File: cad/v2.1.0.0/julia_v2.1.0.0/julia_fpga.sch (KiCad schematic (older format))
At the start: 28 parts, among them U1 EP4CE6F17, X1 50MHz

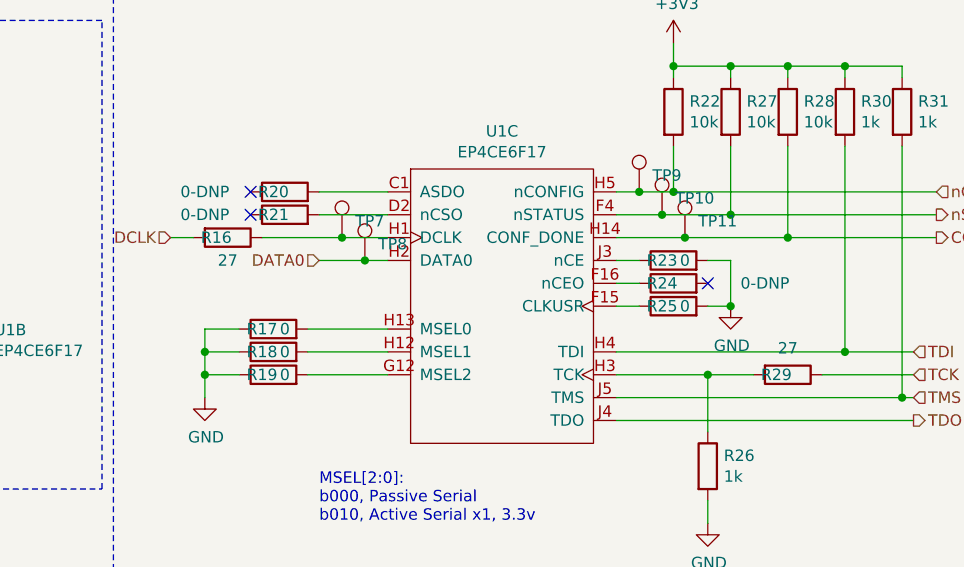
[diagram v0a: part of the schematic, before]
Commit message: v2.1.0.0: changed connector, ERC, annotation/footprint assignment
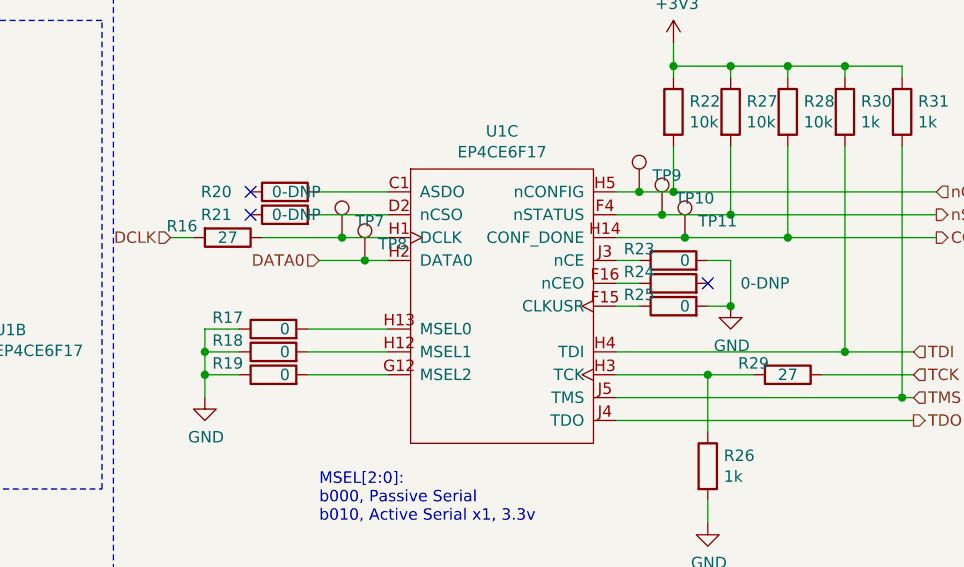
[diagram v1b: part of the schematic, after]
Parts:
- C46: footprint (none) -> Capacitor_Tantalum_SMD:CP_EIA-2012-15_AVX-P
- C47: footprint (none) -> Capacitor_SMD:C_0402_1005Metric
- FB1: footprint (none) -> Inductor_SMD:L_0603_1608Metric
- R15, R16, R17, R18, R19, R20, R21, R22, R23, R24, R25, R26, R27, R28, R29, R30, R31: footprint (none) -> Resistor_SMD:R_0402_1005Metric
- TP10, TP11, TP6, TP7, TP8, TP9: footprint (none) -> TestPoint:TestPoint_THTPad_D1.0mm_Drill0.5mm
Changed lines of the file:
@@
 F 0 "TP6" H 5758 1672 50  0000 L CNN
 F 1 "TestPoint" H 5758 1627 50  0001 L CNN
-F 2 "" H 5900 1600 50  0001 C CNN
+F 2 "TestPoint:TestPoint_THTPad_D1.0mm_Drill0.5mm" H 5900 1600 50  0001 C CNN
 F 3 "~" H 5900 1600 50  0001 C CNN
 	1    5700 1600
@@
 F 0 "C46" H 3518 1796 50  0000 L CNN
 F 1 "4.7uF" H 3518 1705 50  0000 L CNN
-F 2 "" H 3438 1600 50  0001 C CNN
+F 2 "Capacitor_Tantalum_SMD:CP_EIA-2012-15_AVX-P" H 3438 1600 50  0001 C CNN
 F 3 "~" H 3400 1750 50  0001 C CNN
 	1    3400 1750
@@
 F 0 "C47" H 3965 1796 50  0000 L CNN
 F 1 "0.1uF" H 3965 1705 50  0000 L CNN
-F 2 "" H 3888 1600 50  0001 C CNN
+F 2 "Capacitor_SMD:C_0402_1005Metric" H 3888 1600 50  0001 C CNN
 F 3 "~" H 3850 1750 50  0001 C CNN
 	1    3850 1750
@@
 F 0 "FB1" H 3500 1346 50  0000 L CNN
 F 1 "600R/1A" H 3500 1255 50  0000 L CNN
-F 2 "" V 3330 1300 50  0001 C CNN
+F 2 "Inductor_SMD:L_0603_1608Metric" V 3330 1300 50  0001 C CNN
 F 3 "~" H 3400 1300 50  0001 C CNN
 	1    3400 1300
@@
 F 0 "R15" V 5193 1850 50  0000 C CNN
 F 1 "27" V 5284 1850 50  0000 C CNN
-F 2 "" V 5330 1850 50  0001 C CNN
+F 2 "Resistor_SMD:R_0402_1005Metric" V 5330 1850 50  0001 C CNN
 F 3 "~" H 5400 1850 50  0001 C CNN
 	1    5400 1850
@@
 F 0 "TP9" H 9408 1572 50  0000 L CNN
 F 1 "TestPoint" H 9408 1527 50  0001 L CNN
-F 2 "" H 9550 1500 50  0001 C CNN
+F 2 "TestPoint:TestPoint_THTPad_D1.0mm_Drill0.5mm" H 9550 1500 50  0001 C CNN
 F 3 "~" H 9550 1500 50  0001 C CNN
 	1    9350 1500
@@
 F 0 "TP11" H 9608 1772 50  0000 L CNN
 F 1 "TestPoint" H 9608 1727 50  0001 L CNN
-F 2 "" H 9750 1700 50  0001 C CNN
+F 2 "TestPoint:TestPoint_THTPad_D1.0mm_Drill0.5mm" H 9750 1700 50  0001 C CNN
 F 3 "~" H 9750 1700 50  0001 C CNN
 	1    9550 1700
@@
 F 0 "TP10" H 9508 1672 50  0000 L CNN
 F 1 "TestPoint" H 9508 1627 50  0001 L CNN
-F 2 "" H 9650 1600 50  0001 C CNN
+F 2 "TestPoint:TestPoint_THTPad_D1.0mm_Drill0.5mm" H 9650 1600 50  0001 C CNN
 F 3 "~" H 9650 1600 50  0001 C CNN
 	1    9450 1600
@@
 U 1 1 604BBA22
 P 10000 2300
-F 0 "R29" V 10000 2250 50  0000 C CNN
-F 1 "27" V 9884 2300 50  0000 C CNN
-F 2 "" V 9930 2300 50  0001 C CNN
+F 0 "R29" V 9950 2150 50  0000 C CNN
+F 1 "27" V 10000 2300 50  0000 C CNN
+F 2 "Resistor_SMD:R_0402_1005Metric" V 9930 2300 50  0001 C CNN
 F 3 "~" H 10000 2300 50  0001 C CNN
 	1    10000 2300
@@
 F 0 "R26" H 9720 2746 50  0000 L CNN
 F 1 "1k" H 9720 2655 50  0000 L CNN
-F 2 "" V 9580 2700 50  0001 C CNN
+F 2 "Resistor_SMD:R_0402_1005Metric" V 9580 2700 50  0001 C CNN
 F 3 "~" H 9650 2700 50  0001 C CNN
 	1    9650 2700
@@
 F 0 "R30" H 10320 1196 50  0000 L CNN
 F 1 "1k" H 10320 1105 50  0000 L CNN
-F 2 "" V 10180 1150 50  0001 C CNN
+F 2 "Resistor_SMD:R_0402_1005Metric" V 10180 1150 50  0001 C CNN
 F 3 "~" H 10250 1150 50  0001 C CNN
 	1    10250 1150
@@
 F 0 "R31" H 10570 1196 50  0000 L CNN
 F 1 "1k" H 10570 1105 50  0000 L CNN
-F 2 "" V 10430 1150 50  0001 C CNN
+F 2 "Resistor_SMD:R_0402_1005Metric" V 10430 1150 50  0001 C CNN
 F 3 "~" H 10500 1150 50  0001 C CNN
 	1    10500 1150
@@
 U 1 1 60569DDE
 P 7750 2100
-F 0 "R17" V 7750 2150 50  0000 C CNN
+F 0 "R17" V 7800 2300 50  0000 C CNN
 F 1 "0" V 7750 2050 50  0000 C CNN
-F 2 "" V 7680 2100 50  0001 C CNN
+F 2 "Resistor_SMD:R_0402_1005Metric" V 7680 2100 50  0001 C CNN
 F 3 "~" H 7750 2100 50  0001 C CNN
 	1    7750 2100
@@
 U 1 1 60576BC4
 P 7750 2200
-F 0 "R18" V 7750 2250 50  0000 C CNN
+F 0 "R18" V 7800 2400 50  0000 C CNN
 F 1 "0" V 7750 2150 50  0000 C CNN
-F 2 "" V 7680 2200 50  0001 C CNN
+F 2 "Resistor_SMD:R_0402_1005Metric" V 7680 2200 50  0001 C CNN
 F 3 "~" H 7750 2200 50  0001 C CNN
 	1    7750 2200
@@
 U 1 1 605775E4
 P 7750 2300
-F 0 "R19" V 7750 2350 50  0000 C CNN
+F 0 "R19" V 7800 2500 50  0000 C CNN
 F 1 "0" V 7750 2250 50  0000 C CNN
-F 2 "" V 7680 2300 50  0001 C CNN
+F 2 "Resistor_SMD:R_0402_1005Metric" V 7680 2300 50  0001 C CNN
 F 3 "~" H 7750 2300 50  0001 C CNN
 	1    7750 2300
@@
 U 1 1 60584DE0
 P 7800 1500
-F 0 "R20" V 7800 1550 50  0000 C CNN
-F 1 "0-DNP" V 7800 1850 50  0000 C CNN
-F 2 "" V 7730 1500 50  0001 C CNN
+F 0 "R20" V 7800 1800 50  0000 C CNN
+F 1 "0-DNP" V 7800 1450 50  0000 C CNN
+F 2 "Resistor_SMD:R_0402_1005Metric" V 7730 1500 50  0001 C CNN
 F 3 "~" H 7800 1500 50  0001 C CNN
 	1    7800 1500
@@
 U 1 1 60585A79
 P 7800 1600
-F 0 "R21" V 7800 1650 50  0000 C CNN
-F 1 "0-DNP" V 7800 1950 50  0000 C CNN
-F 2 "" V 7730 1600 50  0001 C CNN
+F 0 "R21" V 7800 1900 50  0000 C CNN
+F 1 "0-DNP" V 7800 1550 50  0000 C CNN
+F 2 "Resistor_SMD:R_0402_1005Metric" V 7730 1600 50  0001 C CNN
 F 3 "~" H 7800 1600 50  0001 C CNN
 	1    7800 1600
@@
 U 1 1 6059C913
 P 9500 1800
-F 0 "R23" V 9500 1850 50  0000 C CNN
+F 0 "R23" V 9550 1950 50  0000 C CNN
 F 1 "0" V 9500 1750 50  0000 C CNN
-F 2 "" V 9430 1800 50  0001 C CNN
+F 2 "Resistor_SMD:R_0402_1005Metric" V 9430 1800 50  0001 C CNN
 F 3 "~" H 9500 1800 50  0001 C CNN
 	1    9500 1800
@@
 U 1 1 605A24FE
 P 9500 2000
-F 0 "R25" V 9500 2050 50  0000 C CNN
+F 0 "R25" V 9550 2150 50  0000 C CNN
 F 1 "0" V 9500 1950 50  0000 C CNN
-F 2 "" V 9430 2000 50  0001 C CNN
+F 2 "Resistor_SMD:R_0402_1005Metric" V 9430 2000 50  0001 C CNN
 F 3 "~" H 9500 2000 50  0001 C CNN
 	1    9500 2000
@@
 F 0 "TP7" H 8108 1772 50  0000 L CNN
 F 1 "TestPoint" H 8108 1727 50  0001 L CNN
-F 2 "" H 8250 1700 50  0001 C CNN
+F 2 "TestPoint:TestPoint_THTPad_D1.0mm_Drill0.5mm" H 8250 1700 50  0001 C CNN
 F 3 "~" H 8250 1700 50  0001 C CNN
 	1    8050 1700
@@
 F 0 "TP8" H 8208 1872 50  0000 L CNN
 F 1 "TestPoint" H 8208 1827 50  0001 L CNN
-F 2 "" H 8350 1800 50  0001 C CNN
+F 2 "TestPoint:TestPoint_THTPad_D1.0mm_Drill0.5mm" H 8350 1800 50  0001 C CNN
 F 3 "~" H 8350 1800 50  0001 C CNN
 	1    8150 1800
@@
 U 1 1 6060B39D
 P 7550 1700
-F 0 "R16" V 7550 1650 50  0000 C CNN
-F 1 "27" V 7650 1700 50  0000 C CNN
-F 2 "" V 7480 1700 50  0001 C CNN
+F 0 "R16" V 7500 1500 50  0000 C CNN
+F 1 "27" V 7550 1700 50  0000 C CNN
+F 2 "Resistor_SMD:R_0402_1005Metric" V 7480 1700 50  0001 C CNN
 F 3 "~" H 7550 1700 50  0001 C CNN
 	1    7550 1700
@@
 F 0 "R28" H 10070 1196 50  0000 L CNN
 F 1 "10k" H 10070 1105 50  0000 L CNN
-F 2 "" V 9930 1150 50  0001 C CNN
+F 2 "Resistor_SMD:R_0402_1005Metric" V 9930 1150 50  0001 C CNN
 F 3 "~" H 10000 1150 50  0001 C CNN
 	1    10000 1150
@@
 F 0 "R27" H 9820 1196 50  0000 L CNN
 F 1 "10k" H 9820 1105 50  0000 L CNN
-F 2 "" V 9680 1150 50  0001 C CNN
+F 2 "Resistor_SMD:R_0402_1005Metric" V 9680 1150 50  0001 C CNN
 F 3 "~" H 9750 1150 50  0001 C CNN
 	1    9750 1150
@@
 F 0 "R22" H 9570 1196 50  0000 L CNN
 F 1 "10k" H 9570 1105 50  0000 L CNN
-F 2 "" V 9430 1150 50  0001 C CNN
+F 2 "Resistor_SMD:R_0402_1005Metric" V 9430 1150 50  0001 C CNN
 F 3 "~" H 9500 1150 50  0001 C CNN
 	1    9500 1150
@@
 U 1 1 60597CE6
 P 9500 1900
-F 0 "R24" V 9500 1950 50  0000 C CNN
+F 0 "R24" V 9550 2050 50  0000 C CNN
 F 1 "0-DNP" V 9500 1500 50  0000 C CNN
-F 2 "" V 9430 1900 50  0001 C CNN
+F 2 "Resistor_SMD:R_0402_1005Metric" V 9430 1900 50  0001 C CNN
 F 3 "~" H 9500 1900 50  0001 C CNN
 	1    9500 1900
@@
 Wire Wire Line
 	2200 5650 2550 5650
-Wire Bus Line
-	2650 5750 2650 6900
-Wire Bus Line
-	850  4850 850  6900
-Wire Bus Line
-	5400 4000 5400 5500
-Wire Bus Line
-	4900 3950 4900 5950
-Wire Bus Line
-	3100 3500 3100 5950
 Text Label 2250 5750 0    50   ~ 0
 RGB14
@@
 Wire Wire Line
 	3400 1450 3400 1500
+Wire Bus Line
+	2650 5750 2650 6900
+Wire Bus Line
+	850  4850 850  6900
+Wire Bus Line
+	5400 4000 5400 5500
+Wire Bus Line
+	4900 3950 4900 5950
+Wire Bus Line
+	3100 3500 3100 5950
 $EndSCHEMATC

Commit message: Layout begun
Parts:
- removed R17, R19: 0, Resistor_SMD:R_0402_1005Metric, symbol Device:R
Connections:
- net A0: now also U1.F10 (IO7_F10); no longer U1.T12 (IO4_T12)
- net A1: now also U1.J12 (IO5_J12); no longer U1.R12 (IO4_R12)
- net A10: now also U1.F11 (IO7_F11); no longer U1.T9 (IO4_T9)
- net A11: now also U1.K11 (IO5_K11); no longer U1.R9 (IO4_R9)
- net A2: now also U1.E11 (IO7_E11); no longer U1.T11 (IO4_T11)
- net A3: now also U1.F13 (IO6_F13); no longer U1.R11 (IO4_R11)
- net A4: now also U1.J14 (IO5_J14); no longer U1.T10 (IO4_T10)
- net A5: now also U1.J15 (IO5_J15); no longer U1.R10 (IO4_R10)
- net A6: now also U1.G11 (IO6_G11); no longer U1.N9 (IO4_N9)
- net A7: now also U1.J16 (IO5_J16); no longer U1.M9 (IO4_M9)
- net A8: now also U1.J13 (IO5_J13); no longer U1.L9 (IO4_L9)
- net A9: now also U1.K12 (IO5_K12); no longer U1.K9 (IO4_K9)
- net BA0: now also U1.P15 (IO5_P15); no longer U1.M11 (IO4_M11)
- net BA1: now also U1.J11 (IO5_J11); no longer U1.N12 (IO4_N12)
- net CAS_N: now also U1.P14 (IO4_P14); no longer U1.P9 (IO4_P9)
- net DEN: now also U1.D11 (IO7_D11); no longer U1.B14 (IO7_B14)
- net DQ0: now also U1.T13 (IO4_T13); no longer U1.B16 (IO6_B16)
- net DQ1: now also U1.T14 (IO4_T14); no longer U1.C15 (IO6_C15)
- net DQ10: now also U1.L16 (IO5_L16); no longer U1.K12 (IO5_K12)
- net DQ11: now also U1.N15 (IO5_N15); no longer U1.K15 (IO5_K15)
- net DQ12: now also U1.N14 (IO5_N14); no longer U1.K16 (IO5_K16)
- net DQ13: now also U1.N16 (IO5_N16); no longer U1.L13 (IO5_L13)
- net DQ14: now also U1.N12 (IO4_N12); no longer U1.L14 (IO5_L14)
- net DQ15: now also U1.N13 (IO5_N13); no longer U1.L15 (IO5_L15)
- net DQ16: now also U1.B16 (IO6_B16); no longer U1.L16 (IO5_L16)
- net DQ17: now also U1.A15 (IO7_A15); no longer U1.M12 (IO5_M12)
- net DQ18: now also U1.A14 (IO7_A14); no longer U1.N13 (IO5_N13)
- net DQ19: now also U1.B13 (IO7_B13); no longer U1.N14 (IO5_N14)
- net DQ2: now also U1.R11 (IO4_R11); no longer U1.C16 (IO6_C16)
- net DQ20: now also U1.B12 (IO7_B12); no longer U1.L12 (IO5_L12)
- net DQ21: now also U1.B14 (IO7_B14); no longer U1.P15 (IO5_P15)
- net DQ22: now also U1.A13 (IO7_A13); no longer U1.P16 (IO5_P16)
- net DQ23: now also U1.A12 (IO7_A12); no longer U1.J16 (IO5_J16)
- net DQ24: now also U1.C15 (IO6_C15); no longer U1.J11 (IO5_J11)
- net DQ25: now also U1.C14 (IO7_C14); no longer U1.J15 (IO5_J15)
- net DQ26: now also U1.C16 (IO6_C16); no longer U1.J14 (IO5_J14)
- net DQ27: now also U1.D15 (IO6_D15); no longer U1.J12 (IO5_J12)
- net DQ28: now also U1.D14 (IO7_D14); no longer U1.J13 (IO5_J13)
- net DQ29: now also U1.D16 (IO6_D16); no longer U1.R16 (IO5_R16)
- net DQ3: now also U1.R12 (IO4_R12); no longer U1.D15 (IO6_D15)
- net DQ30: now also U1.F14 (IO6_F14); no longer U1.N16 (IO5_N16)
- net DQ31: now also U1.G15 (IO6_G15); no longer U1.N15 (IO5_N15)
- net DQ4: now also U1.T12 (IO4_T12); no longer U1.D16 (IO6_D16)
- net DQ5: now also U1.T15 (IO4_T15); no longer U1.F13 (IO6_F13)
- net DQ6: now also U1.R13 (IO4_R13); no longer U1.G11 (IO6_G11)
- net DQ7: now also U1.R16 (IO5_R16); no longer U1.G15 (IO6_G15)
- net DQ8: now also U1.L15 (IO5_L15); no longer U1.G16 (IO6_G16)
- net DQ9: now also U1.M12 (IO5_M12); no longer U1.K11 (IO5_K11)
- net DQM0: now also U1.L12 (IO5_L12); no longer U1.T14 (IO4_T14)
- net DQM1: now also U1.L14 (IO5_L14); no longer U1.N11 (IO4_N11)
- net DQM2: now also U1.E10 (IO7_E10); no longer U1.M10 (IO4_M10)
- net DQM3: now also U1.G16 (IO6_G16); no longer U1.T13 (IO4_T13)
- net GND: now also U1.G12 (MSEL2), U1.H13 (MSEL0)
- net HSD: now also U1.B10 (IO7_B10); no longer U1.B13 (IO7_B13)
- net RAS_N: now also U1.L13 (IO5_L13); no longer U1.P11 (IO4_P11)
- net RGB0: now also U1.A2 (IO8_A2); no longer U1.A8 (IO8_A8)
- net RGB1: now also U1.D3 (IO8_D3); no longer U1.B8 (IO8_B8)
- net RGB10: now also U1.D6 (IO8_D6); no longer U1.C6 (IO8_C6)
- net RGB13: now also U1.F6 (IO8_F6); no longer U1.A5 (IO8_A5)
- net RGB14: now also U1.C6 (IO8_C6); no longer U1.A2 (IO8_A2)
- net RGB15: now also U1.F7 (IO8_F7); no longer U1.B5 (IO8_B5)
- net RGB16: now also U1.A7 (IO8_A7); no longer U1.A4 (IO8_A4)
- net RGB17: now also U1.B7 (IO8_B7); no longer U1.B4 (IO8_B4)
- net RGB18: now also U1.D8 (IO8_D8); no longer U1.D5 (IO8_D5)
- net RGB19: now also U1.A8 (IO8_A8); no longer U1.D6 (IO8_D6)
- net RGB2: now also U1.A3 (IO8_A3); no longer U1.C8 (IO8_C8)
- net RGB20: now also U1.B8 (IO8_B8); no longer U1.A3 (IO8_A3)
- net RGB21: now also U1.E8 (IO8_E8); no longer U1.B3 (IO8_B3)
- net RGB22: now also U1.C8 (IO8_C8); no longer U1.C3 (IO8_C3)
- net RGB23: now also U1.F8 (IO8_F8); no longer U1.D3 (IO8_D3)
- net RGB3: now also U1.B3 (IO8_B3); no longer U1.D8 (IO8_D8)
- net RGB4: now also U1.C3 (IO8_C3); no longer U1.E8 (IO8_E8)
- net RGB5: now also U1.A4 (IO8_A4); no longer U1.F8 (IO8_F8)
- net RGB6: now also U1.B4 (IO8_B4); no longer U1.A7 (IO8_A7)
- net RGB7: now also U1.D5 (IO8_D5); no longer U1.B7 (IO8_B7)
- net RGB8: now also U1.A5 (IO8_A5); no longer U1.F6 (IO8_F6)
- net RGB9: now also U1.B5 (IO8_B5); no longer U1.F7 (IO8_F7)
- net SCL: now also U1.B9 (IO7_B9); no longer U1.A11 (IO7_A11)
- net SDA: now also U1.D9 (IO7_D9); no longer U1.B12 (IO7_B12)
- net SDRAM_CKE: now also U1.K16 (IO5_K16); no longer U1.K10 (IO4_K10)
- net SDRAM_CLK: now also U1.K15 (IO5_K15); no longer U1.T15 (IO4_T15)
- net SDRAM_CS_N: now also U1.P16 (IO5_P16); no longer U1.R13 (IO4_R13)
- net SDRAM_WE_N: now also U1.R14 (IO4_R14); no longer U1.L10 (IO4_L10)
- net STBYB: now also U1.A10 (IO7_A10); no longer U1.A13 (IO7_A13)
- net TOUCH_INTN: now also U1.C9 (IO7_C9); no longer U1.A12 (IO7_A12)
- net TOUCH_RSTN: now also U1.A9 (IO7_A9); no longer U1.E10 (IO7_E10)
- net UART1_RX: now also U1.T11 (IO4_T11); no longer U1.F5 (IO1_F5)
- net UART1_TX: now also U1.T10 (IO4_T10); no longer U1.E5 (IO1_E5)
- net VSD: now also U1.A11 (IO7_A11); no longer U1.A14 (IO7_A14)
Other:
- note added: "K15 <-> DPCLK4"
- note removed: "T15<->DPCLK3"

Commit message: Layout complete(?)
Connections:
- net DEN: now also U1.A11 (IO7_A11); no longer U1.D11 (IO7_D11)
- net SCL: now also U1.D9 (IO7_D9); no longer U1.B9 (IO7_B9)
- net SDA: now also U1.C9 (IO7_C9); no longer U1.D9 (IO7_D9)
- net TOUCH_INTN: now also U1.B9 (IO7_B9); no longer U1.C9 (IO7_C9)
- net VSD: now also U1.D11 (IO7_D11); no longer U1.A11 (IO7_A11)
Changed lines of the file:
@@
 Text HLabel 2950 4300 2    50   Output ~ 0
 HSD
+Text HLabel 1600 3800 0    50   Output ~ 0
+VSD
 Text HLabel 1600 4800 0    50   Output ~ 0
-VSD
-Text HLabel 1600 3800 0    50   Output ~ 0
 DEN
 Text HLabel 8050 4400 0    50   Output ~ 0
 LIGHT
-Text HLabel 3000 4400 2    50   Input ~ 0
+Text HLabel 3000 4800 2    50   Input ~ 0
 TOUCH_INTN
 Text HLabel 2800 5100 0    50   Output ~ 0
 TOUCH_RSTN
-Text HLabel 3000 4500 2    50   BiDi ~ 0
+Text HLabel 3000 4400 2    50   BiDi ~ 0
 SDA
-Text HLabel 2650 5000 0    50   Output ~ 0
+Text HLabel 3000 4500 2    50   Output ~ 0
 SCL
 Text HLabel 2950 4200 2    50   Output ~ 0
@@
 	2900 5100 2800 5100
 Wire Wire Line
-	2800 4800 2850 4800
-Wire Wire Line
-	2850 4800 2850 5000
-Wire Wire Line
-	2850 5000 2650 5000
-Wire Wire Line
 	3000 4400 2800 4400
 Wire Wire Line
@@
 Wire Wire Line
 	5800 5400 5700 5400
+Wire Wire Line
+	2800 4800 3000 4800
 Wire Bus Line
 	4900 3950 4900 5950
